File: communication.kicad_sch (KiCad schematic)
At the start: 16 parts, among them X1 ASCO

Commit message: first power management layout iteration, added footprints and values to parts that had none
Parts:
- C113, C114, C117, C69, C73: footprint (none) -> Capacitor_SMD:C_0402_1005Metric
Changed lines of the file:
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@@
       (effects (font (size 1.27 1.27)) (justify right))
     )
-    (property "Footprint" "" (at 143.51 76.2 0)
+    (property "Footprint" "Capacitor_SMD:C_0402_1005Metric" (at 143.51 76.2 0)
       (effects (font (size 1.27 1.27)) hide)
     )
@@
       (effects (font (size 1.27 1.27)) (justify right))
     )
-    (property "Footprint" "" (at 143.51 127 0)
+    (property "Footprint" "Capacitor_SMD:C_0402_1005Metric" (at 143.51 127 0)
       (effects (font (size 1.27 1.27)) hide)
     )
@@
       (effects (font (size 1.27 1.27)) (justify right))
     )
-    (property "Footprint" "" (at 152.4 127 0)
+    (property "Footprint" "Capacitor_SMD:C_0402_1005Metric" (at 152.4 127 0)
       (effects (font (size 1.27 1.27)) hide)
     )
@@
       (effects (font (size 1.27 1.27)) (justify right))
     )
-    (property "Footprint" "" (at 21.59 40.64 0)
+    (property "Footprint" "Capacitor_SMD:C_0402_1005Metric" (at 21.59 40.64 0)
       (effects (font (size 1.27 1.27)) hide)
     )
@@
       (effects (font (size 1.27 1.27)) (justify right))
     )
-    (property "Footprint" "" (at 132.08 76.2 0)
-      (effects (font (size 1.27 1.27)) hide)
-    )
+    (property "Footprint" "Capacitor_SMD:C_0402_1005Metric" (at 132.08 76.2 0)
+      (effects (font (size 1.27 1.27)) hide)
+    )

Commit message: Add missing footprints to components
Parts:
- AE1: LCSC (none) -> C5137195
- L8, L9: footprint (none) -> Inductor_SMD:L_0201_0603Metric
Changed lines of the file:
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@@
       (effects (font (size 1.27 1.27)) (justify left))
     )
-    (property "Footprint" "" (at 135.89 149.86 0)
+    (property "Footprint" "Inductor_SMD:L_0201_0603Metric" (at 135.89 149.86 0)
       (effects (font (size 1.27 1.27)) hide)
     )
@@
       (effects (font (size 1.27 1.27)) hide)
     )
+    (property "LCSC" "C5137195" (at 143.51 97.79 0)
+      (effects (font (size 1.27 1.27)) hide)
+    )
     (pin "1")
     (instances
@@
       (effects (font (size 1.27 1.27)))
     )
-    (property "Footprint" "" (at 137.16 72.39 0)
+    (property "Footprint" "Inductor_SMD:L_0201_0603Metric" (at 137.16 72.39 0)
       (effects (font (size 1.27 1.27)) hide)
     )

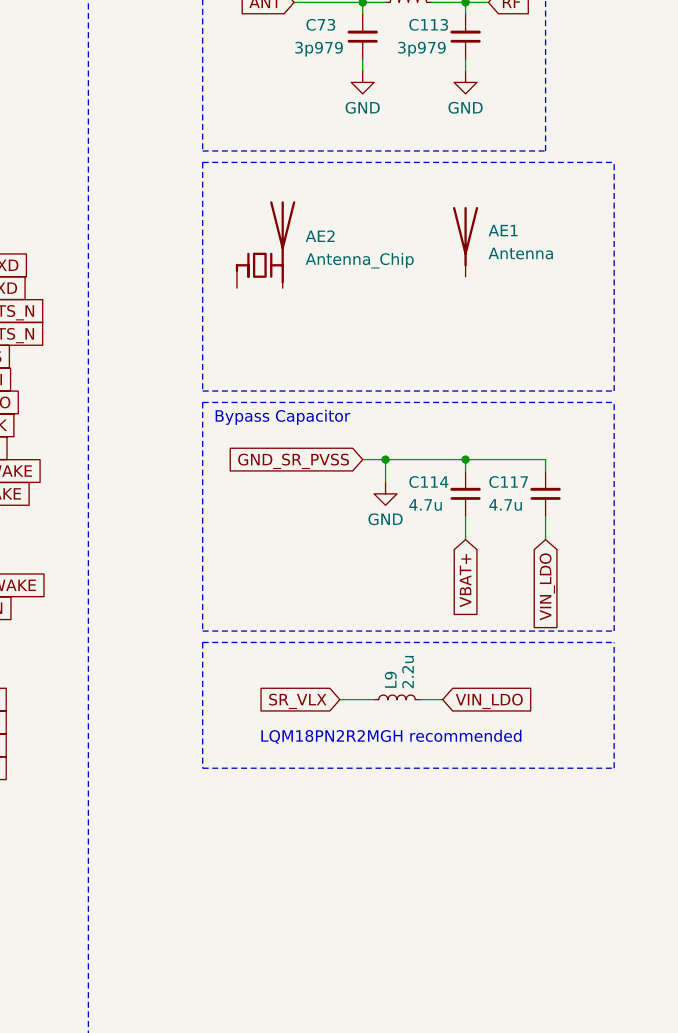
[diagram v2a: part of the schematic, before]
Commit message: added antenna footprints + solder jumper
removed gba.kicad_pro
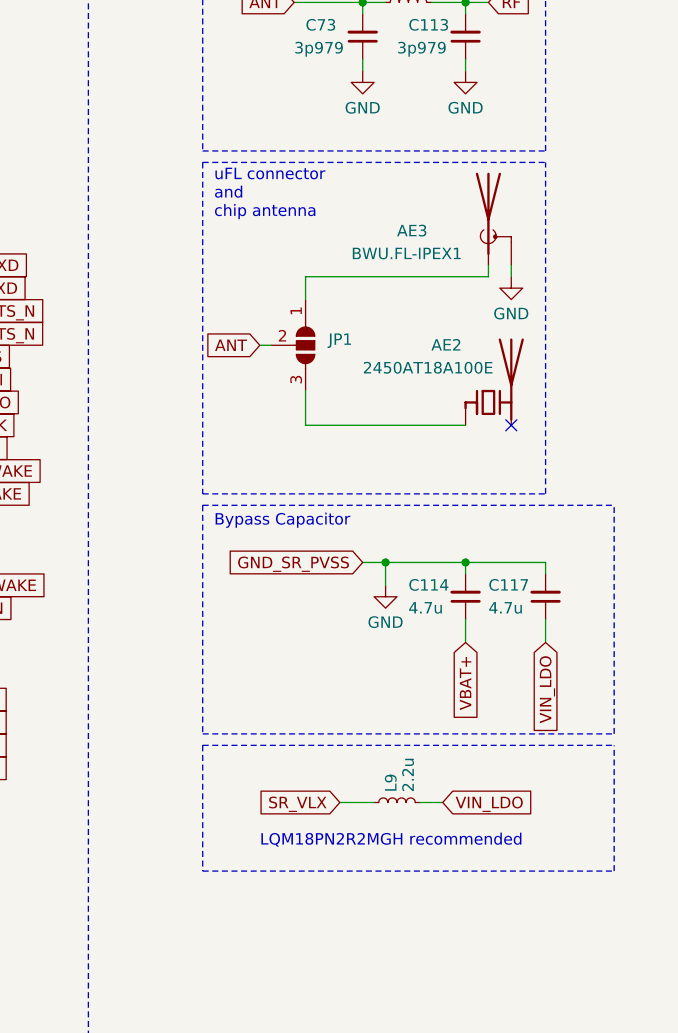
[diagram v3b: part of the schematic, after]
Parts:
- removed AE1: Antenna, symbol Device:Antenna
- added AE3: BWU.FL-IPEX1, ARMband:uFL_antenna, symbol Device:Antenna_Shield
- added JP1: ~, Jumper:SolderJumper-3_P1.3mm_Open_RoundedPad1.0x1.5mm, symbol Jumper:SolderJumper_3_Open
- AE2: value Antenna_Chip -> 2450AT18A100E; footprint (none) -> Resistor_SMD:R_1206_3216Metric; LCSC (none) -> C89334
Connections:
- net ANT: now also JP1.2 (C)
- net GND: now also AE3.2 (Shield)
- net at AE2.1 (FEED): now also JP1.3 (B)
- new net: AE3.1 (A), JP1.1 (A)
- no-connect marks 2 -> 3
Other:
- note added: "uFL connector and chip antenna"
- moved on the sheet: AE2, C114, C117, L9
